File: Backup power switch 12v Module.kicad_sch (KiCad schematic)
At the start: 22 parts, among them J2 External, J5 Esternal, J9 PWR SELECTOR, K1 SRD-12VDC-SL-C, Q3 BSS138, U7 ESP32-C3 Pro Mini, U8 AMS1117-3.3

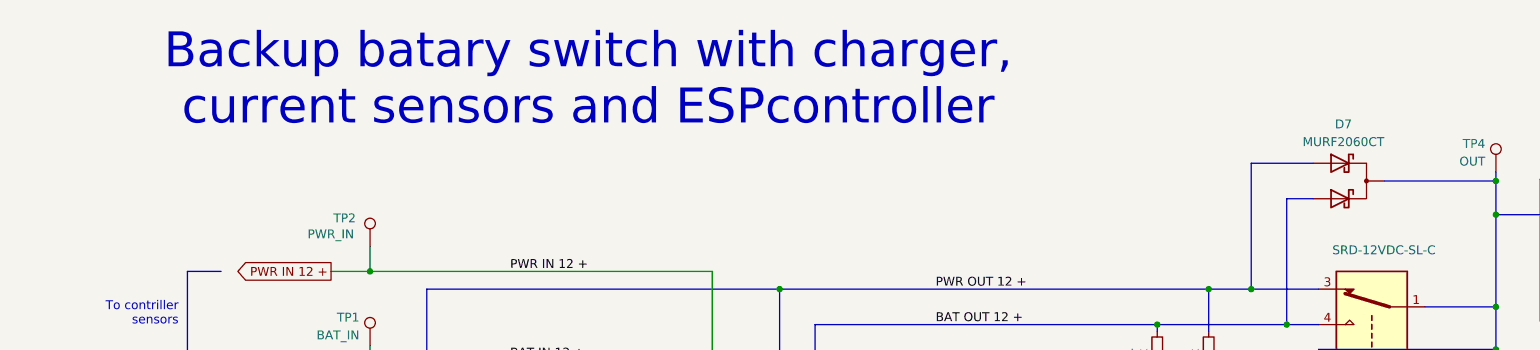
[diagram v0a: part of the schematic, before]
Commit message: Add poert switch
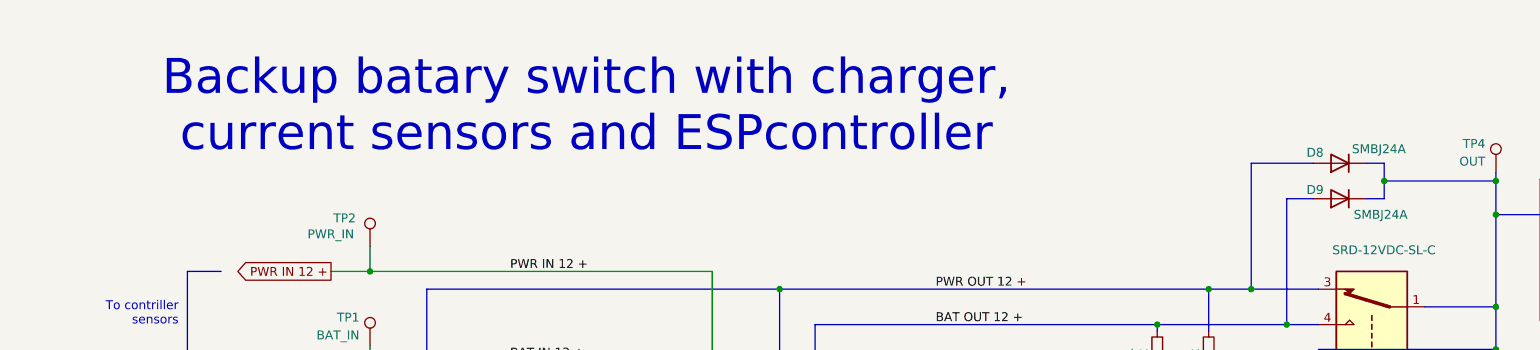
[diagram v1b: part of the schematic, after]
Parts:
- removed D7: MURF2060CT, PCM_Package_TO_SOT_THT_AKL_OneLayer:TO-220-3_Staggered_Vertical, symbol Diode:C3D20065D
- added D8, D9: SMBJ24A, Diode_SMD:D_SMB, symbol Device:D
